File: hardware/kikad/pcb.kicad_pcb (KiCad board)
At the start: 2 copper layers, 45 x 45 mm, 22 parts, among them J1 LED, J2 BOARD

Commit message: organization
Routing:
- net GND: track 177.9 -> 0.00 mm
- net /B: track 98.1 -> 0.00 mm
- net /G: track 83.9 -> 0.00 mm
- net /R: track 81.1 -> 0.00 mm
- net Net-(J1-Pin_6): track 30.7 -> 0.00 mm
- net Net-(J1-Pin_5): track 28.5 -> 0.00 mm
- net Net-(D5-RA): track 11.0 -> 0.00 mm
- net Net-(D4-RA): track 10.9 -> 0.00 mm
- net Net-(D1-BA): track 9.63 -> 0.00 mm
- net Net-(D3-BA): track 9.57 -> 0.00 mm
- net Net-(D2-RA): track 9.49 -> 0.00 mm
- net Net-(D5-GA): track 8.10 -> 0.00 mm
- net Net-(D1-GA): track 7.76 -> 0.00 mm
- net Net-(D3-GA): track 7.62 -> 0.00 mm
- net Net-(D4-GA): track 5.82 -> 0.00 mm
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
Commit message: version 0.2
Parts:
- removed D5: LED_RKGB, LED_THT:LED_D5.0mm-4_RGB_Wide_Pins
- removed J1: LED, Connector_PinSocket_2.54mm:PinSocket_1x06_P2.54mm_Vertical
- added D7: LED_Dual_AKA, Connector_JST:JST_XH_B3B-XH-A_1x03_P2.50mm_Vertical, B.Cu at (114.0, 73.4)
- D1, D2, D3, D4, R1, R10, R11, R12, R13, R14, R2, R3, R4, R5, R6, R7, R8, R9: moved to B.Cu
- U1: footprint esp_32_c3_supper_mini:esp_32_c3_supper_mini -> esp_32_c3_supper_mini:esp_32_c3_supper_mini_tht_smd; moved to B.Cu
- moved J2 14.0 mm to (149.7, 75.6), turned to -90 degrees
- moved R14 9.94 mm to (128.2, 67.1), turned to 180 degrees
- moved D2 6.94 mm to (118.9, 44.6), turned to 180 degrees
- moved D4 6.51 mm to (119.1, 80.6), turned to 180 degrees
- moved D3 5.92 mm to (152.5, 80.6), turned to 180 degrees
- moved D1 5.92 mm to (152.5, 44.6), turned to 180 degrees
- moved R4 5.69 mm to (129.3, 46.8)
- moved R3 5.49 mm to (136.2, 46.8)
- moved R7 5.05 mm to (135.6, 78.4)
- moved R10 5.05 mm to (129.7, 78.3)
- moved R9 4.30 mm to (135.6, 82.8)
- moved R13 4.27 mm to (120.6, 69.6), turned to 0 degrees
- moved U1 4.11 mm to (141.9, 63.1)
- moved R12 4.02 mm to (129.7, 82.8)
- moved R1 3.42 mm to (136.2, 42.4)
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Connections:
- R13 pad 1: Net-(J1-Pin_6) -> Net-(D7-A1)
- R13 pad 2: Net-(D5-GA) -> Net-(U1-GPIO6)
- R14 pad 1: Net-(D5-RA) -> Net-(U1-GPIO5)
- R14 pad 2: Net-(J1-Pin_5) -> Net-(D7-A2)
- U1 pad 10: Net-(J1-Pin_6) -> Net-(U1-GPIO6)
- U1 pad 9: Net-(J1-Pin_5) -> Net-(U1-GPIO5)
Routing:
- net GND: track 0.00 -> 158.4 mm
- net /R: track 0.00 -> 72.6 mm
- net /G: track 0.00 -> 63.7 mm
- net /B: track 0.00 -> 54.8 mm
- net Net-(U1-GPIO5): track 0.00 -> 41.3 mm
- net Net-(U1-GPIO6): track 0.00 -> 37.9 mm
- net Net-(D4-BA): track 0.00 -> 10.4 mm
- net Net-(D3-RA): track 0.00 -> 10.2 mm
- net Net-(D2-BA): track 0.00 -> 10.1 mm
- net Net-(D1-RA): track 0.00 -> 9.61 mm
- net Net-(D2-GA): track 0.00 -> 8.57 mm
- net Net-(D4-GA): track 0.00 -> 8.29 mm
- net Net-(D7-A1): track 0.00 -> 8.16 mm
- net Net-(D7-A2): track 0.00 -> 7.12 mm
- net Net-(D3-GA): track 0.00 -> 5.99 mm
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- added copper zone on F.Cu, net GND
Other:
- board text added: "LED_TEST_BOARD_V_0_2"
- board text removed: "5V+"
- board text removed: "GND"
- board text removed: "LED_TEST_BOARD_V_0_1"
- board text removed: "MR MG"
- board text removed: "R G B"

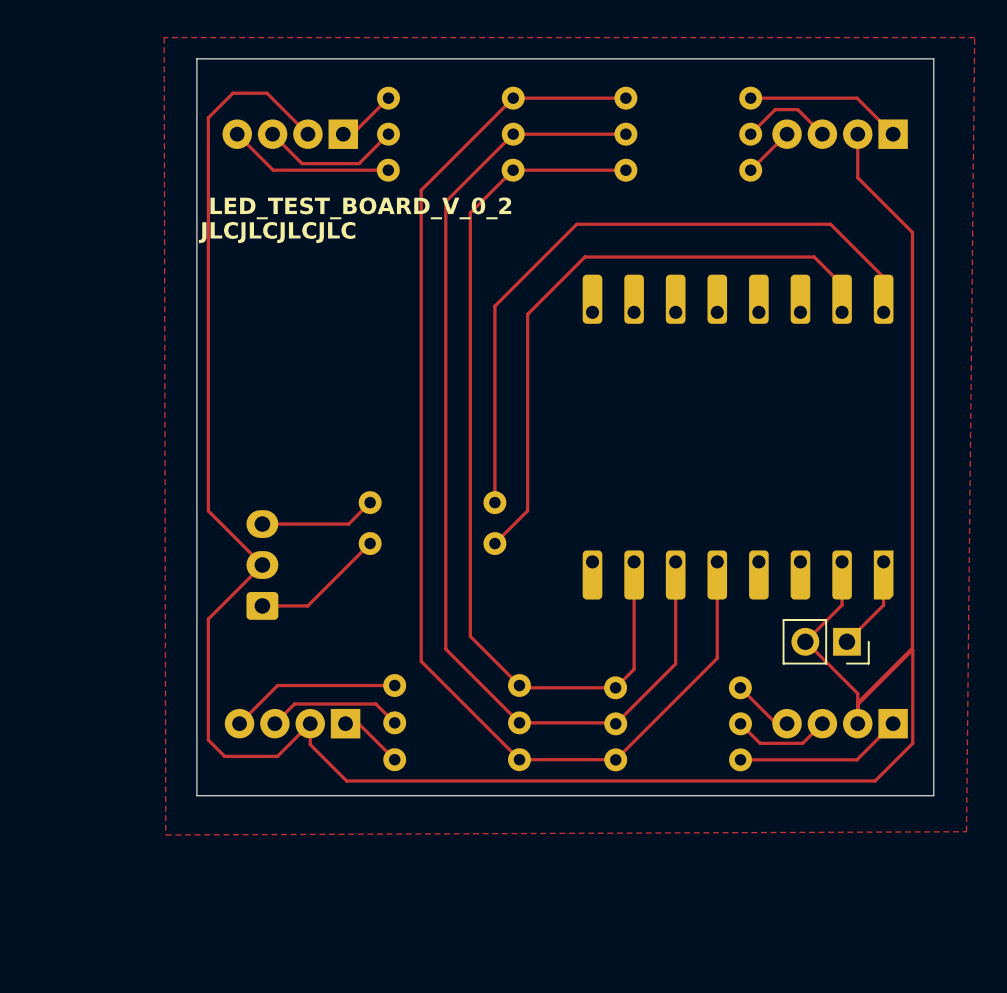
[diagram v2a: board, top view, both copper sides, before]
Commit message: works nfc reader
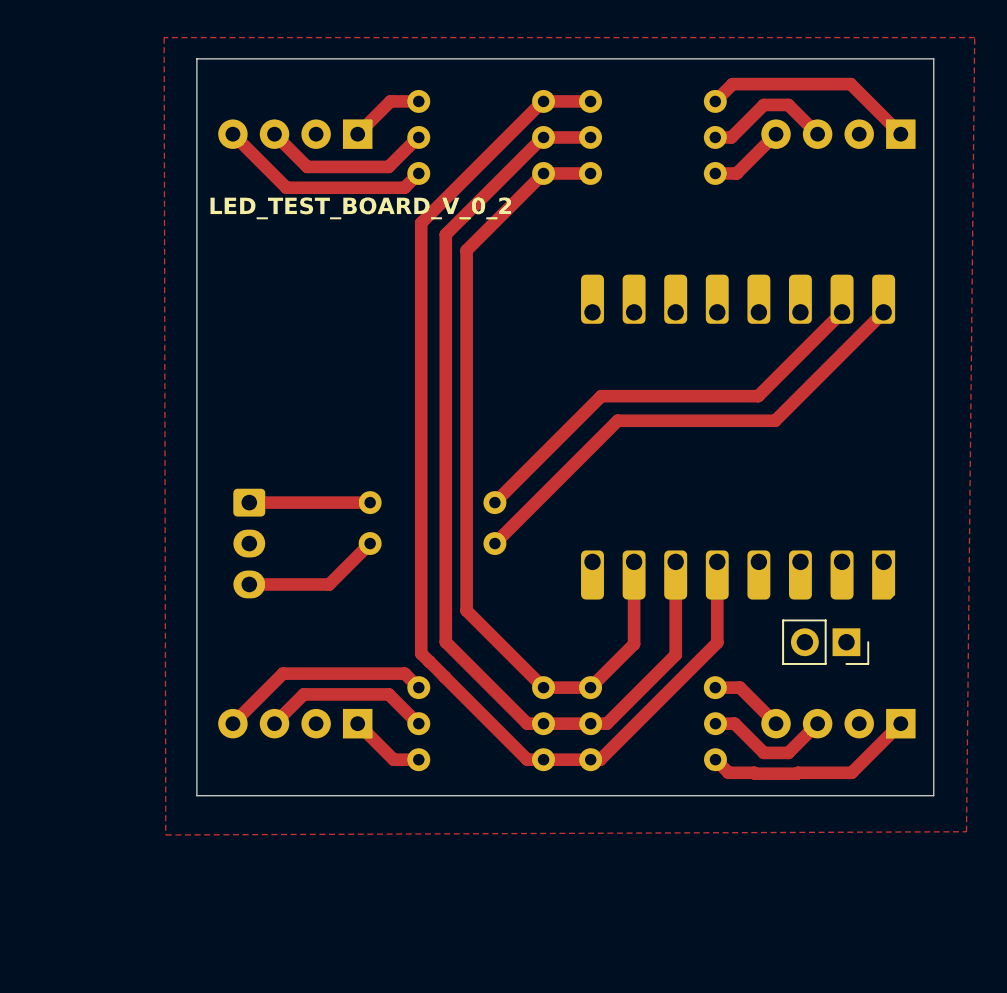
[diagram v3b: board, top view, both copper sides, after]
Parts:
- D1, D2, D3, D4: footprint LED_THT:LED_D5.0mm-4_RGB_Wide_Pins -> LED_THT:LED_D5.0mm-4_RGB_Wide_Pins_custom
- moved D7 6.36 mm to (113.2, 67.1), turned to -90 degrees
- moved R13 2.50 mm to (120.6, 67.1)
- moved R14 2.50 mm to (128.2, 69.6)
- moved R1 2.17 mm to (134.0, 42.6)
- moved R3 2.17 mm to (134.0, 47.0)
- moved R2 2.17 mm to (134.0, 44.8)
- moved R4 1.87 mm to (131.2, 47.0)
- moved R6 1.86 mm to (131.2, 42.6)
- moved R5 1.86 mm to (131.2, 44.8)
- moved R7 1.53 mm to (134.0, 78.4)
- moved R8 1.53 mm to (134.1, 80.6)
- moved R9 1.53 mm to (134.1, 82.8)
- moved R10 1.48 mm to (131.2, 78.4)
- moved R11 1.47 mm to (131.2, 80.6)
- moved R12 1.47 mm to (131.2, 82.8)
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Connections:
- U1 pad 1: Net-(J2-Pin_1) -> (no net)
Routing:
- net GND: track 158.4 -> 0.00 mm
- net Net-(U1-GPIO6): track 37.9 -> 26.0 mm
- net Net-(U1-GPIO5): track 41.3 -> 29.6 mm
- net Net-(J2-Pin_1): track 5.81 -> 0.00 mm
- net /B: track 54.8 -> 49.8 mm
- net /R: track 72.6 -> 68.4 mm
- net /G: track 63.7 -> 59.7 mm
- net Net-(D1-RA): track 9.61 -> 13.0 mm
- net Net-(D2-BA): track 10.1 -> 13.1 mm
- net Net-(D3-RA): track 10.2 -> 12.9 mm
- net Net-(D4-BA): track 10.4 -> 13.0 mm
- net Net-(D1-GA): track 5.62 -> 7.81 mm
- net Net-(D4-GA): track 8.29 -> 10.3 mm
- net Net-(D2-GA): track 8.57 -> 10.4 mm
- net Net-(D3-GA): track 5.99 -> 7.79 mm
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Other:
- board text removed: "JLCJLCJLCJLC"

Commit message: make the v0.3 read to use
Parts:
- removed D7: LED_Dual_AKA, Connector_JST:JST_XH_B3B-XH-A_1x03_P2.50mm_Vertical
- removed J2: BOARD, Connector_PinSocket_2.54mm:PinSocket_1x02_P2.54mm_Vertical
- added BZ1: Buzzer, Buzzer_Beeper:MagneticBuzzer_ProSignal_ABI-010-RC, B.Cu at (144.4, 53.4)
- added J1: Output, Connector_JST:JST_XH_B3B-XH-A_1x03_P2.50mm_Vertical, B.Cu at (151.9, 84.3)
- added U2: ~, esp_32_c3_supper_mini:PN532 NFC RFID, B.Cu at (117.2, 67.5)
- D1, D2, D3, D4: footprint LED_THT:LED_D5.0mm-4_RGB_Wide_Pins_custom -> LED_THT:LED_D5.0mm-4_RGB_Wide_Pins
- R14: value 150 -> 0
- moved R13 22.1 mm to (140.2, 57.0), turned to 90 degrees
- moved D4 15.8 mm to (108.7, 91.8)
- moved R14 15.1 mm to (135.4, 82.8), turned to 0 degrees
- moved D3 13.4 mm to (146.0, 92.1), turned to 0 degrees
- moved R12 13.4 mm to (121.3, 91.8)
- moved R11 13.3 mm to (121.3, 89.6)
- moved R10 13.3 mm to (121.3, 87.3)
- moved R9 10.7 mm to (128.3, 91.8)
- moved D2 10.7 mm to (109.2, 43.4)
- moved R8 10.7 mm to (128.3, 89.6)
- moved R7 10.6 mm to (128.3, 87.3)
- moved R4 10.4 mm to (120.8, 47.1)
- moved R5 10.4 mm to (120.8, 44.9)
- moved R6 10.4 mm to (120.8, 42.6)
- moved U1 7.78 mm to (143.5, 70.7)
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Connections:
- R13 pad 1: Net-(D7-A1) -> Net-(U1-GPIO9/SCL)
- R13 pad 2: Net-(U1-GPIO6) -> Net-(BZ1-+)
- R14 pad 1: Net-(U1-GPIO5) -> Net-(R14-Pad1)
- R14 pad 2: Net-(D7-A2) -> Net-(U1-3V3)
- U1 pad 1: (no net) -> unconnected-(U1-5V-Pad1)
- U1 pad 10: Net-(U1-GPIO6) -> Net-(U1-GPIO6/MOSI)
- U1 pad 11: unconnected-(U1-GPIO7-Pad11) -> Net-(U1-GPIO7/SS)
- U1 pad 12: unconnected-(U1-GPIO8-Pad12) -> Net-(U1-GPIO8/SDA)
- U1 pad 13: unconnected-(U1-GPIO9-Pad13) -> Net-(U1-GPIO9/SCL)
- U1 pad 14: unconnected-(U1-GPIO10-Pad14) -> /R
- U1 pad 15: unconnected-(U1-GPIO20-Pad15) -> /G
- U1 pad 16: unconnected-(U1-GPIO21-Pad16) -> /B
- U1 pad 3: unconnected-(U1-3V3-Pad3) -> Net-(U1-3V3)
- U1 pad 4: unconnected-(U1-GPIO4-Pad4) -> Net-(U1-GPIO4/SCK)
- U1 pad 5: /R -> unconnected-(U1-GPIO3-Pad5)
- U1 pad 6: /G -> Net-(J1-Pin_3)
- U1 pad 7: /B -> Net-(J1-Pin_2)
- U1 pad 9: Net-(U1-GPIO5) -> Net-(U1-GPIO5/MISO)
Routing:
- net /R: track 68.4 -> 105.5 mm
- net /G: track 59.7 -> 91.3 mm
- net /B: track 49.8 -> 80.8 mm
- net Net-(U1-GPIO5): track 29.6 -> 0.00 mm
- net Net-(U1-GPIO5/MISO): track 0.00 -> 27.6 mm
- net Net-(U1-GPIO6): track 26.0 -> 0.00 mm
- net Net-(R14-Pad1): track 0.00 -> 24.4 mm
- net Net-(U1-GPIO6/MOSI): track 0.00 -> 24.0 mm
- net Net-(U1-GPIO8/SDA): track 0.00 -> 21.9 mm
- net Net-(U1-GPIO7/SS): track 0.00 -> 20.4 mm
- net Net-(U1-GPIO4/SCK): track 0.00 -> 18.8 mm
- net Net-(J1-Pin_2): track 0.00 -> 18.6 mm
- net Net-(D3-BA): track 4.62 -> 19.3 mm
- net Net-(D1-BA): track 4.70 -> 17.4 mm
- net Net-(J1-Pin_3): track 0.00 -> 11.9 mm
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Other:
- board size 45 x 45 mm -> 55 x 55 mm
- board text removed: "LED_TEST_BOARD_V_0_2"

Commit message: Revert "make the v0.3 read to use"
This reverts commit 2651ca28fcff3cfeeb4fb146a67662ef7f719936.
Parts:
- removed BZ1: Buzzer, Buzzer_Beeper:MagneticBuzzer_ProSignal_ABI-010-RC
- removed J1: Output, Connector_JST:JST_XH_B3B-XH-A_1x03_P2.50mm_Vertical
- removed U2: ~, esp_32_c3_supper_mini:PN532 NFC RFID
- added D7: LED_Dual_AKA, Connector_JST:JST_XH_B3B-XH-A_1x03_P2.50mm_Vertical, B.Cu at (113.2, 67.1)
- added J2: BOARD, Connector_PinSocket_2.54mm:PinSocket_1x02_P2.54mm_Vertical, F.Cu at (149.7, 75.6)
- D1, D2, D3, D4: footprint LED_THT:LED_D5.0mm-4_RGB_Wide_Pins -> LED_THT:LED_D5.0mm-4_RGB_Wide_Pins_custom
- R14: value 0 -> 150
- moved R13 22.1 mm to (120.6, 67.1), turned to 0 degrees
- moved D4 15.8 mm to (119.8, 80.6)
- moved R14 15.1 mm to (128.2, 69.6), turned to 180 degrees
- moved D3 13.4 mm to (153.0, 80.6), turned to 180 degrees
- moved R12 13.4 mm to (131.2, 82.8)
- moved R11 13.3 mm to (131.2, 80.6)
- moved R10 13.3 mm to (131.2, 78.4)
- moved R9 10.7 mm to (134.1, 82.8)
- moved D2 10.7 mm to (119.8, 44.6)
- moved R8 10.7 mm to (134.1, 80.6)
- moved R7 10.6 mm to (134.0, 78.4)
- moved R4 10.4 mm to (131.2, 47.0)
- moved R5 10.4 mm to (131.2, 44.8)
- moved R6 10.4 mm to (131.2, 42.6)
- moved U1 7.78 mm to (141.9, 63.1)
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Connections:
- R13 pad 1: Net-(U1-GPIO9/SCL) -> Net-(D7-A1)
- R13 pad 2: Net-(BZ1-+) -> Net-(U1-GPIO6)
- R14 pad 1: Net-(R14-Pad1) -> Net-(U1-GPIO5)
- R14 pad 2: Net-(U1-3V3) -> Net-(D7-A2)
- U1 pad 1: unconnected-(U1-5V-Pad1) -> (no net)
- U1 pad 10: Net-(U1-GPIO6/MOSI) -> Net-(U1-GPIO6)
- U1 pad 11: Net-(U1-GPIO7/SS) -> unconnected-(U1-GPIO7-Pad11)
- U1 pad 12: Net-(U1-GPIO8/SDA) -> unconnected-(U1-GPIO8-Pad12)
- U1 pad 13: Net-(U1-GPIO9/SCL) -> unconnected-(U1-GPIO9-Pad13)
- U1 pad 14: /R -> unconnected-(U1-GPIO10-Pad14)
- U1 pad 15: /G -> unconnected-(U1-GPIO20-Pad15)
- U1 pad 16: /B -> unconnected-(U1-GPIO21-Pad16)
- U1 pad 3: Net-(U1-3V3) -> unconnected-(U1-3V3-Pad3)
- U1 pad 4: Net-(U1-GPIO4/SCK) -> unconnected-(U1-GPIO4-Pad4)
- U1 pad 5: unconnected-(U1-GPIO3-Pad5) -> /R
- U1 pad 6: Net-(J1-Pin_3) -> /G
- U1 pad 7: Net-(J1-Pin_2) -> /B
- U1 pad 9: Net-(U1-GPIO5/MISO) -> Net-(U1-GPIO5)
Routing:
- net /R: track 105.5 -> 68.4 mm
- net /G: track 91.3 -> 59.7 mm
- net /B: track 80.8 -> 49.8 mm
- net Net-(U1-GPIO5): track 0.00 -> 29.6 mm
- net Net-(U1-GPIO5/MISO): track 27.6 -> 0.00 mm
- net Net-(U1-GPIO6): track 0.00 -> 26.0 mm
- net Net-(R14-Pad1): track 24.4 -> 0.00 mm
- net Net-(U1-GPIO6/MOSI): track 24.0 -> 0.00 mm
- net Net-(U1-GPIO8/SDA): track 21.9 -> 0.00 mm
- net Net-(U1-GPIO7/SS): track 20.4 -> 0.00 mm
- net Net-(U1-GPIO4/SCK): track 18.8 -> 0.00 mm
- net Net-(J1-Pin_2): track 18.6 -> 0.00 mm
- net Net-(D3-BA): track 19.3 -> 4.62 mm
- net Net-(D1-BA): track 17.4 -> 4.70 mm
- net Net-(J1-Pin_3): track 11.9 -> 0.00 mm
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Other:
- board size 55 x 55 mm -> 45 x 45 mm
- board text added: "LED_TEST_BOARD_V_0_2"
